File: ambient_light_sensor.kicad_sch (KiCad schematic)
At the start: 2 parts

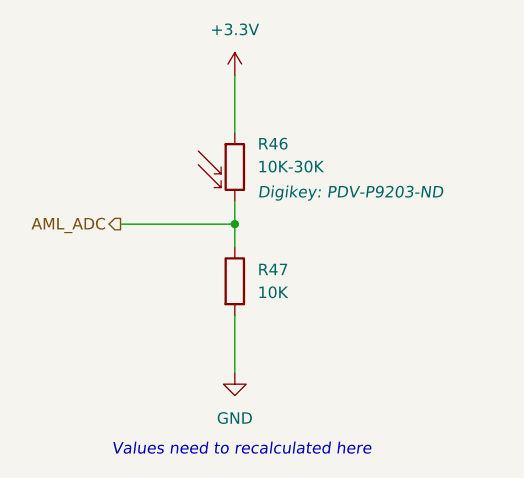
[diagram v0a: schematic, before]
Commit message: change in display module
- Created new sheets
- Reordered the sheets
- Created the footprint for the display
- 3D model of the display
- MCU selection
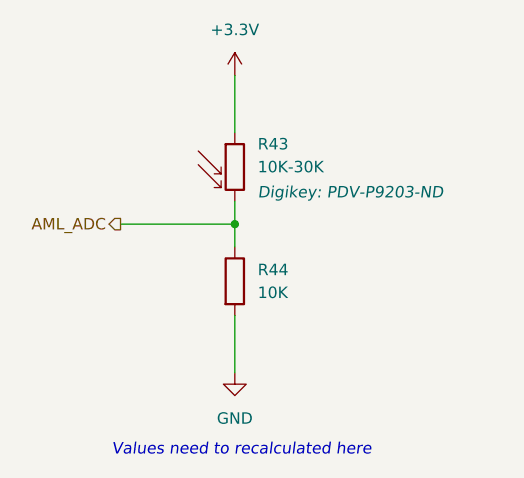
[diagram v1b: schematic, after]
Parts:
- renumbered R46 to R43, R47 to R44
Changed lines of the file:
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@@
 		(dnp no)
 		(fields_autoplaced yes)
-		(property "Reference" "R47"
+		(property "Reference" "R44"
 			(at 148.59 100.3299 0)
 			(effects
@@
 			(project "Precision Clock"
 				(path "/c9a8ff63-a0d1-4125-9dd1-40fb53daf536/2347aac3-442d-482b-8fbc-6e1d41c86b79"
-					(reference "R47")
+					(reference "R44")
 					(unit 1)
 				)
@@
 		(on_board yes)
 		(dnp no)
-		(property "Reference" "R46"
+		(property "Reference" "R43"
 			(at 148.59 86.36 0)
 			(effects
@@
 			)
 		)
-		(property "Datasheet" "https://www.advancedphotonix.com/wp-content/uploads/2015/07/DS-PDV-P9203.pdf"
+		(property "Datasheet" "~"
 			(at 146.05 90.17 0)
 			(effects
@@
 			(project "Precision Clock"
 				(path "/c9a8ff63-a0d1-4125-9dd1-40fb53daf536/2347aac3-442d-482b-8fbc-6e1d41c86b79"
-					(reference "R46")
+					(reference "R43")
 					(unit 1)
 				)
@@
 		(dnp no)
 		(fields_autoplaced yes)
-		(property "Reference" "#PWR033"
+		(property "Reference" "#PWR036"
 			(at 146.05 118.11 0)
 			(effects
@@
 			(project "Precision Clock"
 				(path "/c9a8ff63-a0d1-4125-9dd1-40fb53daf536/2347aac3-442d-482b-8fbc-6e1d41c86b79"
-					(reference "#PWR033")
+					(reference "#PWR036")
 					(unit 1)
 				)
@@
 		(dnp no)
 		(fields_autoplaced yes)
-		(property "Reference" "#PWR08"
+		(property "Reference" "#PWR035"
 			(at 146.05 82.55 0)
 			(effects
@@
 			(project "Precision Clock"
 				(path "/c9a8ff63-a0d1-4125-9dd1-40fb53daf536/2347aac3-442d-482b-8fbc-6e1d41c86b79"
-					(reference "#PWR08")
-					(unit 1)
-				)
+					(reference "#PWR035")
+					(unit 1)
+				)

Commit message: minor changes
- removed the power, ambient light sensing circuits.
- minor changes in the primary MCU pinout.
- USB connector moved to MCU sheet.
- ESD protection added.
- removed the test points from the individual sheets.
- Improved readability.
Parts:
- removed R43: 10K-30K, symbol Device:R_Photo
- removed R44: 10K, symbol Device:R
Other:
- note removed: "Values need to recalculated here"
